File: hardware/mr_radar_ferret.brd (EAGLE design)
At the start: 76.2 x 76.2 mm, 91 parts

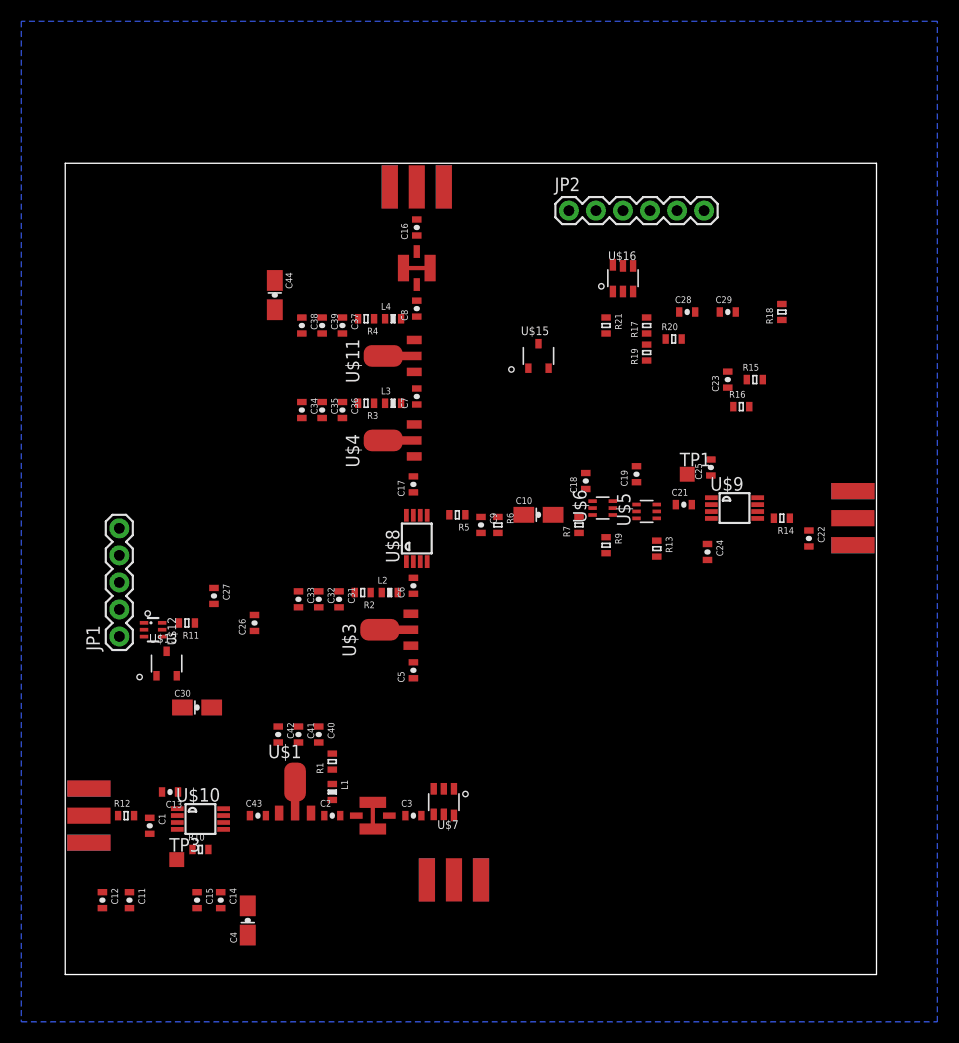
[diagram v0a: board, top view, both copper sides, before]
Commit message: component placement complete on ferret, layout partially complete. silkscreen cleanup and amplifier grounds remain
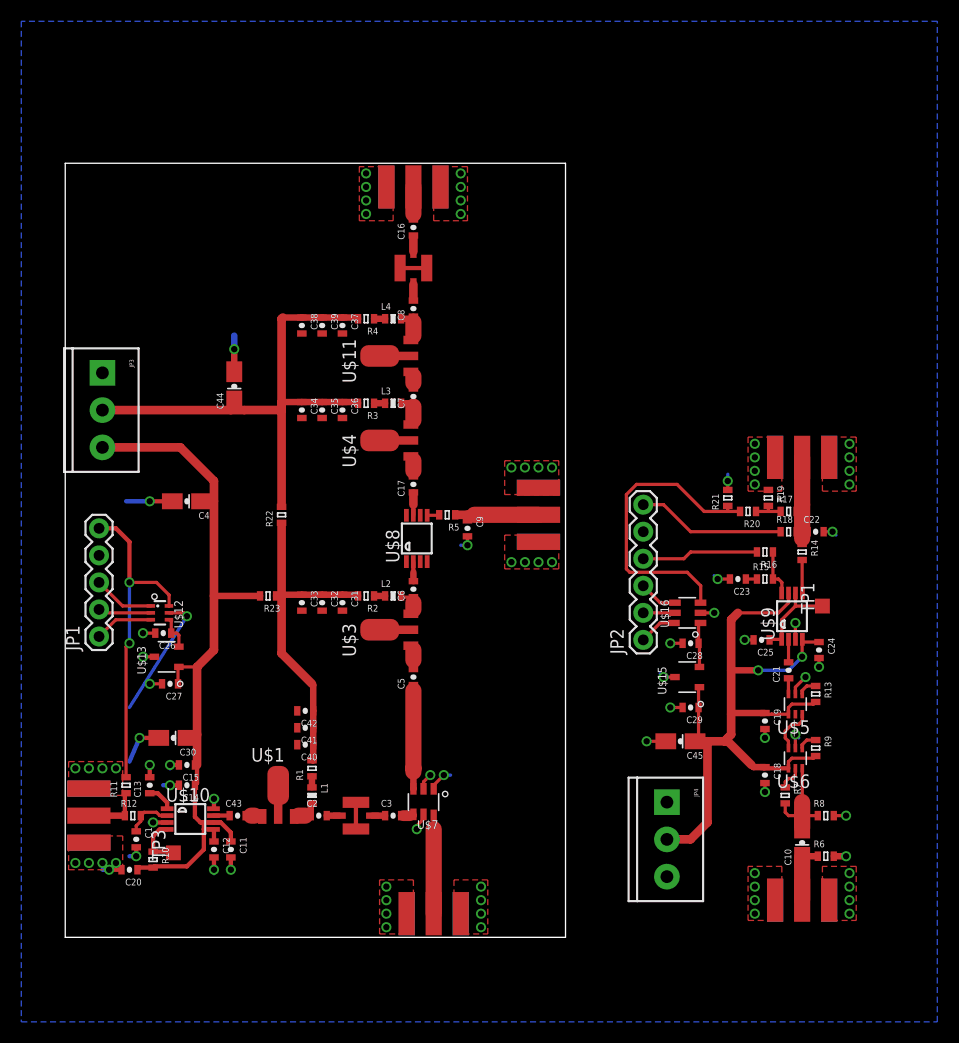
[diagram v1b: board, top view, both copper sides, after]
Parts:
- added C20: 100nF, pel_dipol_comp:0603-CAP
- added C45: 10uF, pel_dipol_comp:3216/A
- added J$5, J$6: SMA_EDGE, SparkFun-Connectors:SMA-EDGE
- added JP3, JP4: (no value), SparkFun-Connectors:SCREWTERMINAL-3.5MM-3
- added R22, R23: 110, pel_dipol_comp:0603-RES
- added R8: 100, pel_dipol_comp:0603-RES
- moved R6 43.8 mm to (71.4, 11.1), turned to 0 degrees
- moved JP2 40.9 mm to (54.3, 31.4), turned to 90 degrees
- moved C4 39.8 mm to (11.4, 44.5), turned to 180 degrees
- moved C10 39.5 mm to (69.2, 12.4), turned to 90 degrees
- moved C29 37.3 mm to (58.7, 25.1), turned to 180 degrees
- moved U$15 33.2 mm to (58.4, 27.9), turned to 90 degrees
- moved C18 32.3 mm to (65.7, 18.7), turned to 270 degrees
- moved U$16 32.0 mm to (58.4, 34.0), turned to 90 degrees
- moved R7 31.9 mm to (67.6, 16.8), turned to 270 degrees
- moved C28 31.1 mm to (58.7, 31.1), turned to 180 degrees
- moved U$6 29.7 mm to (68.6, 20.3), turned to 180 degrees
- moved R9 27.4 mm to (70.5, 21.3)
- moved C19 26.1 mm to (65.7, 23.8), turned to 270 degrees
- moved U$5 22.9 mm to (68.6, 25.4), turned to 180 degrees
- moved R17 22.0 mm to (67.9, 43.5), turned to 0 degrees
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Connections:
- new net N$39: C9.P$1, J$5.SIG, R5.P$1
- new net N$54: JP1.5, R11.P$2, U$12.6
- net +10V: now also JP3.2, R22.P$2; no longer C31.P$1, C32.P$1, C33.P$1, C40.P$1, C41.P$1, C42.P$1, R1.P$2, R2.P$2
- net +5V: now also C20.P$1, C45.+, JP3.3, JP4.2, R23.P$2
- net GND: now also C20.P$2, C45.-, J$5.GND@0, J$5.GND@1, J$5.GND@2, J$5.GND@3, J$6.GND@0, J$6.GND@1, J$6.GND@2, J$6.GND@3, JP3.1, JP4.1, JP4.3, R8.P$2
- net N$1: now also R8.P$1
- net N$23: now also J$6.SIG; no longer C9.P$1, R5.P$1
- net N$25: now also JP2.4; no longer JP2.1
- net N$42: now also JP2.3; no longer JP2.4
- net N$43: now also JP2.1, U$16.6; no longer R11.P$2, U$12.6
- net N$44: now also JP2.2; no longer JP2.3
- net N$48: now also C31.P$1, C32.P$1, C33.P$1, C40.P$1, C41.P$1, C42.P$1, R1.P$2, R2.P$2, R22.P$1, R23.P$1; no longer JP2.2, U$16.6
- net VTUNE: no longer JP1.5
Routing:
- net +5V: track 0.00 -> 139.7 mm, vias 0 -> 2
- net GND: track 0.00 -> 74.4 mm, vias 0 -> 85
- net +10V: track 0.00 -> 53.6 mm
- net N$48: track 0.00 -> 31.5 mm
- net N$54: track 0.00 -> 30.9 mm, vias 0 -> 2
- net N$53: track 0.00 -> 28.9 mm
- net N$51: track 0.00 -> 14.0 mm
- net N$35: track 0.00 -> 11.7 mm
- net N$25: track 0.00 -> 10.9 mm
- net N$10: track 0.00 -> 10.1 mm
- net N$1: track 0.00 -> 9.65 mm
- net N$7: track 0.00 -> 9.23 mm
- net COM: track 0.00 -> 8.58 mm
- net N$39: track 0.00 -> 8.34 mm
- net N$47: track 0.00 -> 5.78 mm
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- added copper zone on layer 1, net GND
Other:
- board size 76.2 x 76.2 mm -> 47 x 72.7 mm

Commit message: split adc front-end to another board, changed microstrip for 1.6mm thick board
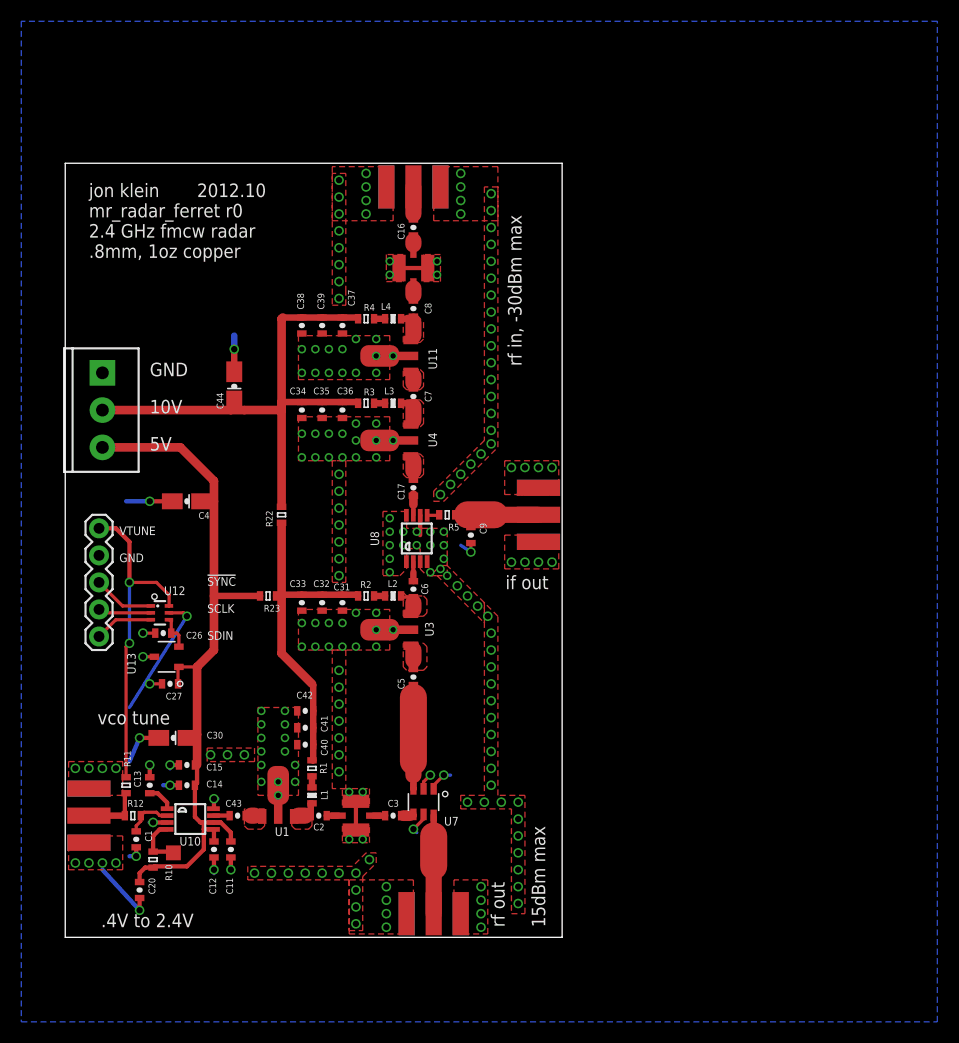
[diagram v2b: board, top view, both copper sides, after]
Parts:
- removed C10, C45: 10uF, pel_dipol_comp:3216/A
- removed C18, C19, C24: 100nF, pel_dipol_comp:0603-CAP
- removed C21: 1uF, pel_dipol_comp:0603-CAP
- removed C22: DNP, pel_dipol_comp:0603-CAP
- removed C23: 2nH, pel_dipol_comp:0603-CAP
- removed C25: 100nH, pel_dipol_comp:0603-CAP
- removed C28, C29: .1uF, pel_dipol_comp:0603-CAP
- removed J$3, J$6: SMA_EDGE, SparkFun-Connectors:SMA-EDGE
- removed JP2: (no value), SparkFun-Connectors:1X06
- removed JP4: (no value), SparkFun-Connectors:SCREWTERMINAL-3.5MM-3
- removed R13, R14, R15, R16, R17, R18, R19, R20, R21, R9: JMP, pel_dipol_comp:0603-RES
- removed R6, R8: 100, pel_dipol_comp:0603-RES
- removed R7: 2k, pel_dipol_comp:0603-RES
- removed TP1: TPTP14SQ, testpad:TP14SQ
- removed U$15: REF2930, retro:SOT23-3
- removed U$16: AD7276, retro:SOT23-6
- removed U$5, U$6: MAX9812, retro:SC70-6
- removed U$9: MAX7410, retro:UMAX8
- moved C20 2.13 mm to (6.99, 7.94), turned to 270 degrees
- moved C9 0.71 mm to (38.1, 41.3)
- moved C17 0.32 mm to (32.7, 45.7)
- renumbered U$1 to U1, U$10 to U10, U$11 to U11, U$12 to U12, U$13 to U13, U$3 to U3, U$4 to U4, U$7 to U7, U$8 to U8
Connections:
- removed net COM: C25.P$1, TP1.TP, U$9.1, U$9.6
- removed net N$1: C10.-, R7.P$2, R8.P$1, U$6.6
- removed net N$23: C10.+, J$6.SIG, R6.P$1
- removed net N$25: JP2.4, R16.P$2
- removed net N$31: R9.P$1, U$6.1
- removed net N$32: R13.P$1, U$5.1
- removed net N$33: C21.P$1, U$5.3
- removed net N$34: C21.P$2, U$9.2
- removed net N$35: C22.P$1, J$3.SIG, R14.P$1, R17.P$2, R18.P$2
- removed net N$36: R14.P$2, U$9.5
- removed net N$37: R15.P$2, R16.P$1, U$9.8
- removed net N$38: C23.P$1, R15.P$1
- removed net N$40: R7.P$1, U$6.5
- removed net N$42: JP2.3, U$16.4
- removed net N$43: JP2.1, U$16.6
- removed net N$44: JP2.2, U$16.5
- removed net N$49: C28.P$1, U$15.2, U$16.1
- removed net N$51: JP2.6, R18.P$1
- removed net N$52: R17.P$1, R19.P$2, R20.P$1
- removed net N$53: R20.P$2, R21.P$1, U$16.3
- removed net N$9: U$5.6, U$6.3
- net +5V: no longer C18.P$1, C19.P$1, C24.P$1, C29.P$1, C45.+, JP4.2, R13.P$2, R9.P$2, U$15.1, U$5.4, U$6.4, U$9.4, U$9.7
- net GND: now also U8.4; no longer C18.P$2, C19.P$2, C22.P$2, C23.P$2, C24.P$2, C25.P$2, C28.P$2, C29.P$2, C45.-, J$3.GND@0, J$3.GND@1, J$3.GND@2, J$3.GND@3, J$6.GND@0, J$6.GND@1, J$6.GND@2, J$6.GND@3, JP2.5, JP4.1, JP4.3, R19.P$1, R21.P$2, R6.P$2, R8.P$2, U$15.3, U$16.2, U$5.2, U$6.2, U$9.3
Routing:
- net +5V: track 139.7 -> 71.3 mm, vias 2 -> 0
- net N$53: track 28.9 -> 0.00 mm
- net N$51: track 14.0 -> 0.00 mm
- net N$35: track 11.7 -> 0.00 mm
- net N$25: track 10.9 -> 0.00 mm
- net N$1: track 9.65 -> 0.00 mm
- net COM: track 8.58 -> 0.00 mm
- net GND: track 74.4 -> 66.5 mm, vias 85 -> 215
- net N$23: track 5.54 -> 0.00 mm
- net N$37: track 4.52 -> 0.00 mm
- net N$9: track 4.34 -> 0.00 mm
- net N$49: track 4.24 -> 0.00 mm
- net N$42: track 3.64 -> 0.00 mm
- net N$43: track 3.54 -> 0.00 mm
- net N$36: track 3.12 -> 0.00 mm
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- added copper zone on layer 1, net N$11
- added copper zone on layer 1, net N$13
- added copper zone on layer 1, net N$18
- added copper zone on layer 1, net N$19
- added copper zone on layer 1, net N$20
- added copper zone on layer 1, net N$29
- added copper zone on layer 1, net N$3
- added copper zone on layer 1, net N$5
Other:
- board size 47 x 72.7 mm -> 46.7 x 72.7 mm
- board text added: "!SYNC"
- board text added: ".4V to 2.4V"
- board text added: ".8mm, 1oz copper"
- board text added: "10V"
- board text added: "15dBm max"
- board text added: "2.4 GHz fmcw radar"
- board text added: "2012.10"
- board text added: "5V"
- board text added: "GND"
- board text added: "SCLK"
- board text added: "SDIN"
- board text added: "VTUNE"
- board text added: "if out"
- board text added: "jon klein"
- board text added: "mr_radar_ferret r0"
- board text added: "rf in, -30dBm max"
- board text added: "rf out"
- board text added: "vco tune"

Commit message: mr_radar_ferret r0, sent for manufacturing
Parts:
- R22: value 110 -> JMP
- R23: value 110 -> DNP
- moved JP3 0.64 mm to (4.13, 56.5)
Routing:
- net +5V: track 71.3 -> 70.7 mm
- net +10V: track 53.6 -> 53.0 mm
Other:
- board text added: "1.6mm, 1oz copper"
- board text removed: ".8mm, 1oz copper"
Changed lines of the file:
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@@
 <text x="12.065" y="5.715" size="1.27" layer="121" font="vector" ratio="16" rot="R180">.4V to 2.4V</text>
 <text x="45.085" y="4.445" size="1.27" layer="121" font="vector" ratio="16" rot="R90">15dBm max</text>
-<text x="2.2225" y="67.31" size="1.27" layer="121" font="vector" ratio="16">.8mm, 1oz copper</text>
+<text x="2.2225" y="67.31" size="1.27" layer="121" font="vector" ratio="16">1.6mm, 1oz copper</text>
 <text x="45.4025" y="37.465" size="1.27" layer="121" font="vector" ratio="16" rot="R180">if out</text>
 <text x="5.08" y="41.275" size="0.8128" layer="121" font="vector" ratio="16">VTUNE</text>
@@
 <element name="C20" library="pel_dipol_comp" package="0603-CAP" value="100nF" x="6.985" y="7.9375" rot="R270"/>
 <element name="J$5" library="SparkFun-Connectors" package="SMA-EDGE" value="SMA_EDGE" x="44.45" y="40.64" rot="R90"/>
-<element name="JP3" library="SparkFun-Connectors" package="SCREWTERMINAL-3.5MM-3" value="" x="3.4925" y="56.515" smashed="yes" rot="R270">
-<attribute name="VALUE" x="4.7625" y="57.785" size="0.4064" layer="27" rot="R270"/>
-</element>
-<element name="R22" library="pel_dipol_comp" package="0603-RES" value="110" x="20.32" y="43.18" rot="R90"/>
-<element name="R23" library="pel_dipol_comp" package="0603-RES" value="110" x="19.05" y="35.56" rot="R180"/>
+<element name="JP3" library="SparkFun-Connectors" package="SCREWTERMINAL-3.5MM-3" value="" x="4.1275" y="56.515" smashed="yes" rot="R270">
+<attribute name="VALUE" x="5.3975" y="57.785" size="0.4064" layer="27" rot="R270"/>
+</element>
+<element name="R22" library="pel_dipol_comp" package="0603-RES" value="JMP" x="20.32" y="43.18" rot="R90"/>
+<element name="R23" library="pel_dipol_comp" package="0603-RES" value="DNP" x="19.05" y="35.56" rot="R180"/>
 </elements>
 <signals>
@@
 <wire x1="24.13" y1="53.7725" x2="22.225" y2="53.7725" width="0.6096" layer="1"/>
 <contactref element="JP3" pad="2"/>
-<wire x1="3.4925" y1="53.015" x2="15.5575" y2="53.015" width="0.8128" layer="1"/>
+<wire x1="4.1275" y1="53.015" x2="15.5575" y2="53.015" width="0.8128" layer="1"/>
 <wire x1="15.5575" y1="53.015" x2="16.82" y2="53.015" width="0.8128" layer="1"/>
 <wire x1="16.8275" y1="53.0225" x2="20.32" y2="53.0225" width="0.8128" layer="1"/>
@@
 <wire x1="13.97" y1="44.45" x2="13.97" y2="46.355" width="0.8128" layer="1"/>
 <wire x1="13.97" y1="46.355" x2="10.81" y2="49.515" width="0.8128" layer="1"/>
-<wire x1="10.81" y1="49.515" x2="3.4925" y2="49.515" width="0.8128" layer="1"/>
+<wire x1="10.81" y1="49.515" x2="4.1275" y2="49.515" width="0.8128" layer="1"/>
 <wire x1="11.535" y1="22.225" x2="11.8525" y2="22.5425" width="0.4064" layer="1"/>
 <wire x1="11.8525" y1="22.5425" x2="12.3825" y2="22.5425" width="0.4064" layer="1"/>
@@
 </signal>
 </signals>
-<errors>
-</errors>
 </board>
 </drawing>
